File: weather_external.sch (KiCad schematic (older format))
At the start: 30 parts, among them J1 Conn_01x02_Male, J2 USB_B_Mini, J3 Conn_01x02_Male, J8 FTDI, Q1 DMG2305UX-13, SW1 SW_Push, U1 MCP73831-2-OT, U2 MCP1700T-3302E_TT

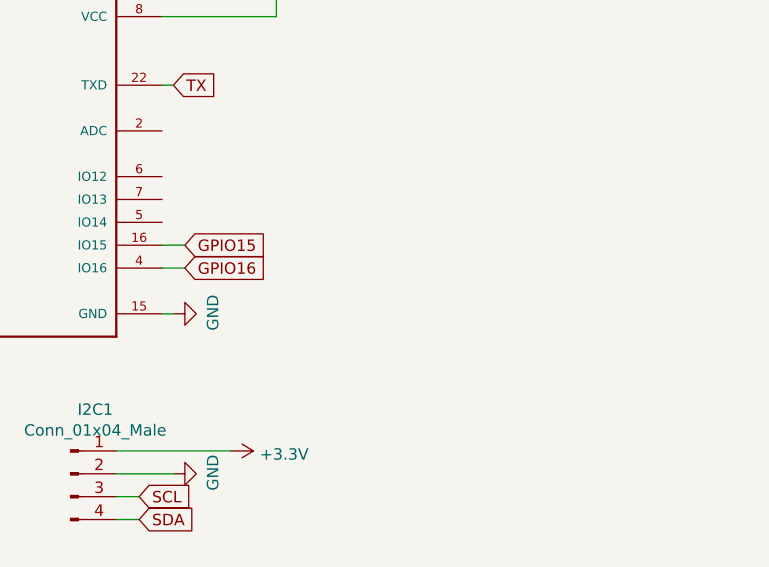
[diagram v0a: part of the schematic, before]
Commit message: V1.4 - adding jumper to reset configurations(wifi and custom)
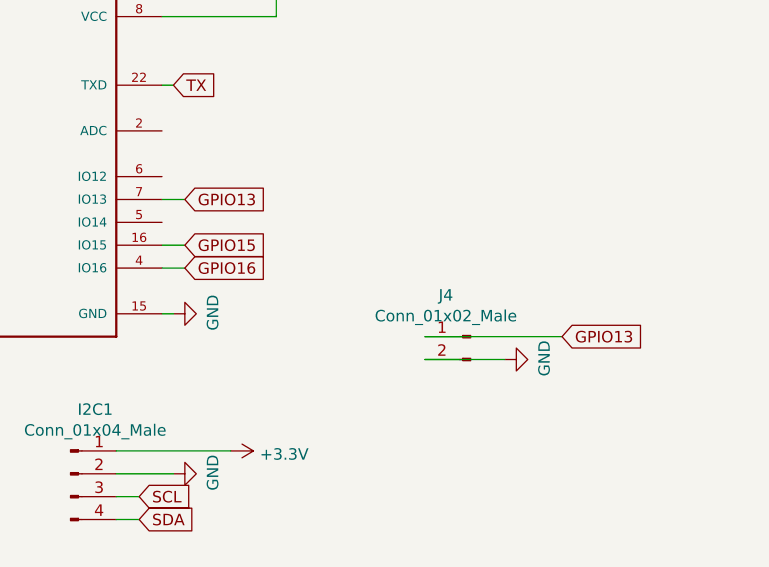
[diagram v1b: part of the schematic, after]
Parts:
- added J4: Conn_01x02_Male, Connector_PinHeader_2.54mm:PinHeader_1x02_P2.54mm_Vertical, symbol Connector:Conn_01x02_Male
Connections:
- net labels added: GPIO13
- wire segments 108 -> 111
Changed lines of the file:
@@
 Wire Wire Line
 	3550 6150 4100 6150
+Text GLabel 7550 3500 2    50   Input ~ 0
+GPIO13
+Wire Wire Line
+	7450 3500 7550 3500
+$Comp
+L Connector:Conn_01x02_Male J4
+U 1 1 5FC5BE4B
+P 8800 4100
+F 0 "J4" H 8908 4281 50  0000 C CNN
+F 1 "Conn_01x02_Male" H 8908 4190 50  0000 C CNN
+F 2 "Connector_PinHeader_2.54mm:PinHeader_1x02_P2.54mm_Vertical" H 8800 4100 50  0001 C CNN
+F 3 "~" H 8800 4100 50  0001 C CNN
+	1    8800 4100
+	-1   0    0    -1
+$EndComp
+$Comp
+L power:GND #PWR0124
+U 1 1 5FC5C799
+P 8950 4200
+F 0 "#PWR0124" H 8950 3950 50  0001 C CNN
+F 1 "GND" H 8955 4027 50  0000 C CNN
+F 2 "" H 8950 4200 50  0001 C CNN
+F 3 "" H 8950 4200 50  0001 C CNN
+	1    8950 4200
+	0    -1   -1   0
+$EndComp
+Wire Wire Line
+	8950 4200 8600 4200
+Text GLabel 9200 4100 2    50   Input ~ 0
+GPIO13
+Wire Wire Line
+	9200 4100 8600 4100
 $EndSCHEMATC
